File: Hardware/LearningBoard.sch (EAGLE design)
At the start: 55 parts, among them IC1 FT230XS-RFT230XS-R

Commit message: Completed first PCB design ready for OSHPark. REmoved alternate PCB design file created only 1.
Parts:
- removed EXTRA: (no value), pinhead:PINHD-2X5
- D_A: device pinhead:PINHD-1X6 -> pinhead:PINHD-1X8
- I2C: device pinhead:PINHD-1X5 -> pinhead:PINHD-1X6
- UART: device pinhead:PINHD-1X4 -> pinhead:PINHD-1X5
- renumbered BTN4 to T_STMP
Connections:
- net N$28 renamed DIN
- removed net N$31: RPU5.2, U$11.OS
- new net OS: I2C.5, RPU5.2, U$11.OS
- new net VDD_I2C: C1.1, I2C.6, RPU16.2, RPU17.2, RPU5.1, U$11.VCC, U$2.VDD
- new net VDD_IR: RECEIVER_.C, RPU12.2, TRANSMITTER.4
- new net VDD_SPI: C3.1, RPU4.1, SPI.7, U$1.VDD
- new net VDD_UART: C10.1, C5.1, C8.1, C9.1, IC1.!RESET, IC1.3V3OUT, IC1.VCC, IC1.VCCIO, UART.5
- net LEFT_BTN: now also D_A.3; no longer D_A.2
- net MISO: now also SPI.4, U$1.SDO; no longer SPI.3, U$1.SDI
- net MOSI: now also SPI.3, U$1.SDI; no longer SPI.4, U$1.SDO
- net POT_OUT: now also D_A.2; no longer D_A.1
- net RIGHT_BTN: now also D_A.5; no longer D_A.3
- net UP_BTN: now also D_A.6; no longer D_A.5
- net VDD: now also D_A.8; no longer C1.1, C10.1, C3.1, C5.1, C8.1, C9.1, EXTRA.10, EXTRA.2, EXTRA.4, EXTRA.6, EXTRA.8, I2C.5, IC1.!RESET, IC1.3V3OUT, IC1.VCC, IC1.VCCIO, RECEIVER_.C, RPU12.2, RPU16.2, RPU17.2, RPU4.1, RPU5.1, SPI.7, TRANSMITTER.4, U$1.VDD, U$11.VCC, U$2.VDD
- net VIN: now also D_A.7; no longer D_A.6
- net VSS: now also D_A.1; no longer EXTRA.1, EXTRA.3, EXTRA.5, EXTRA.7, EXTRA.9
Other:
- note removed: "EXTRA"
- moved on the sheet: DOWN, IC1, LEFT, RIGHT, UP

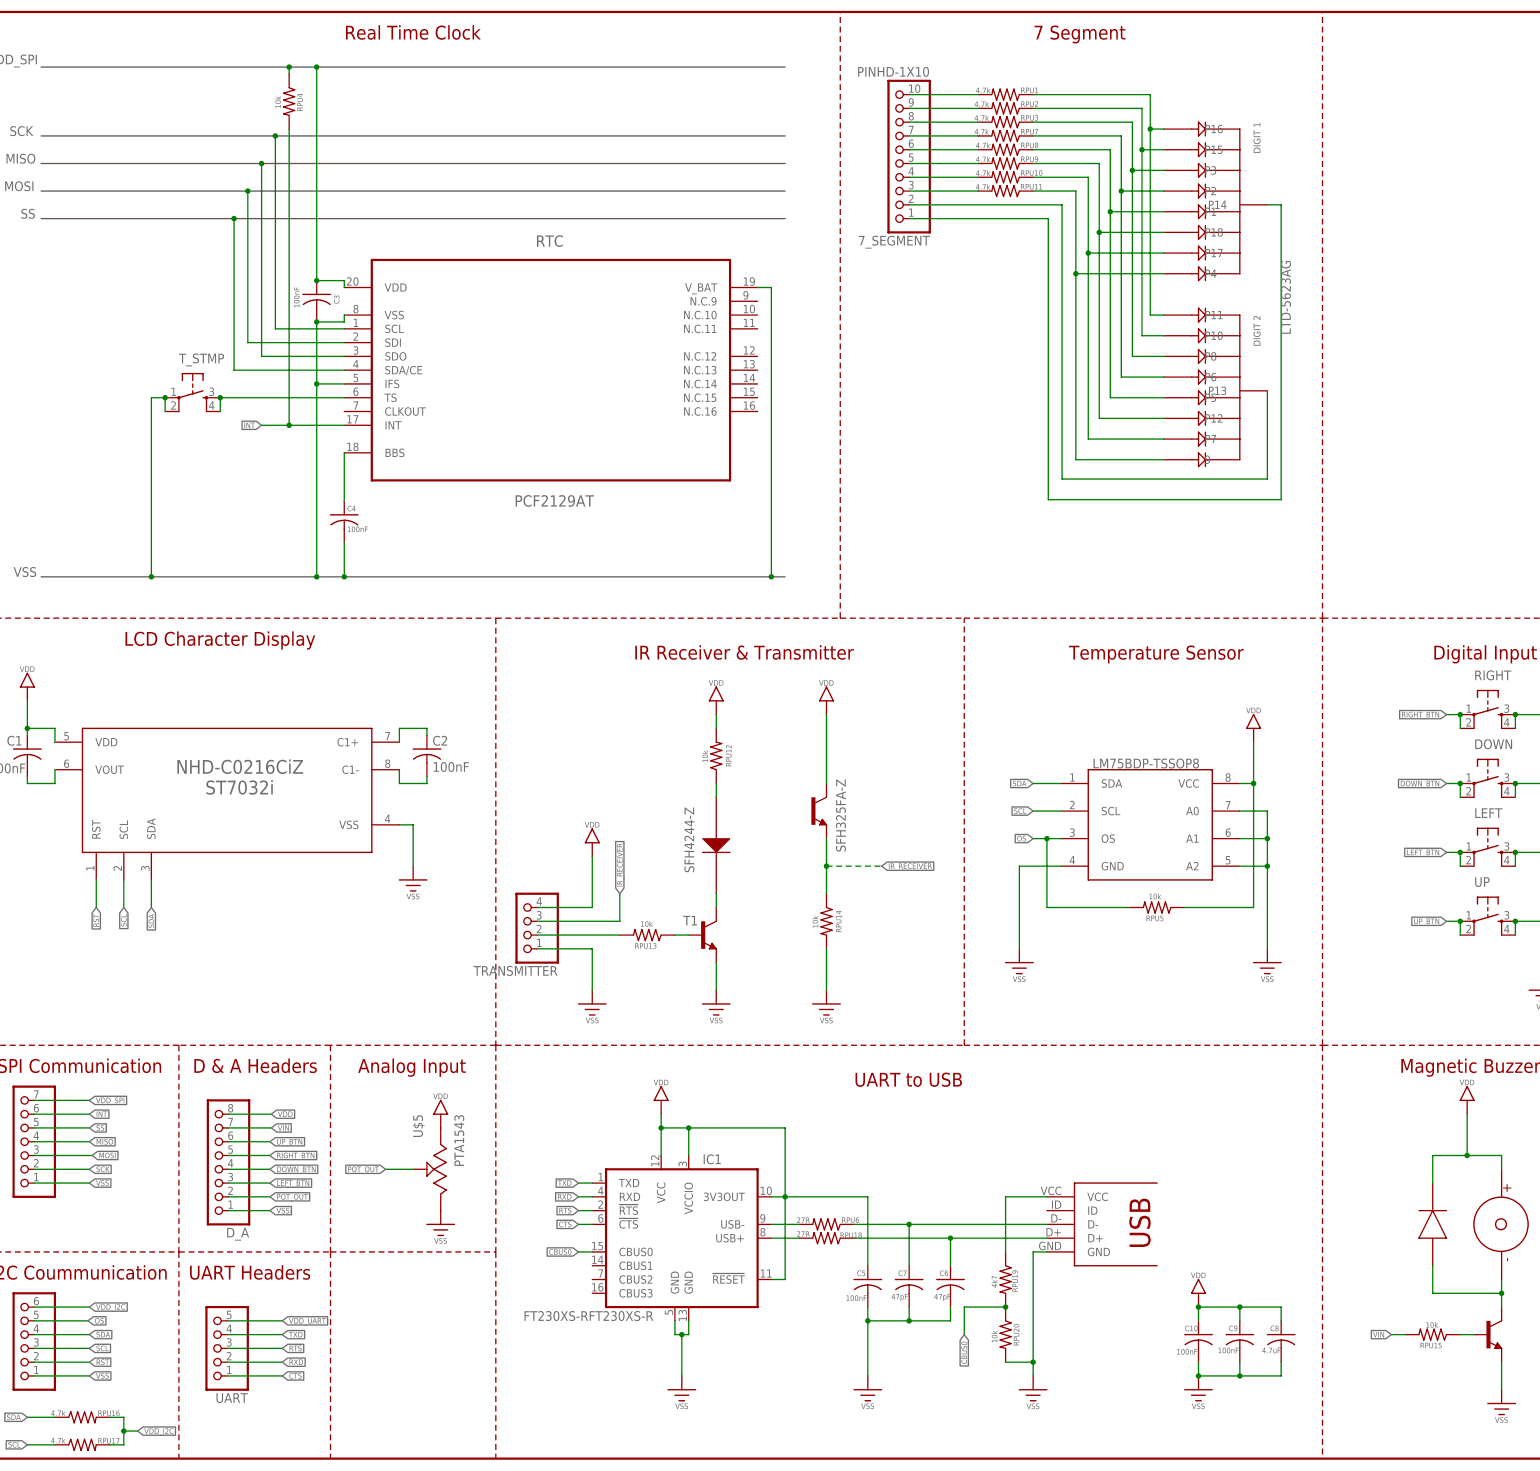
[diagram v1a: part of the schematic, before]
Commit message: - Added some resistor values - Changed resistor names (removed UP string).
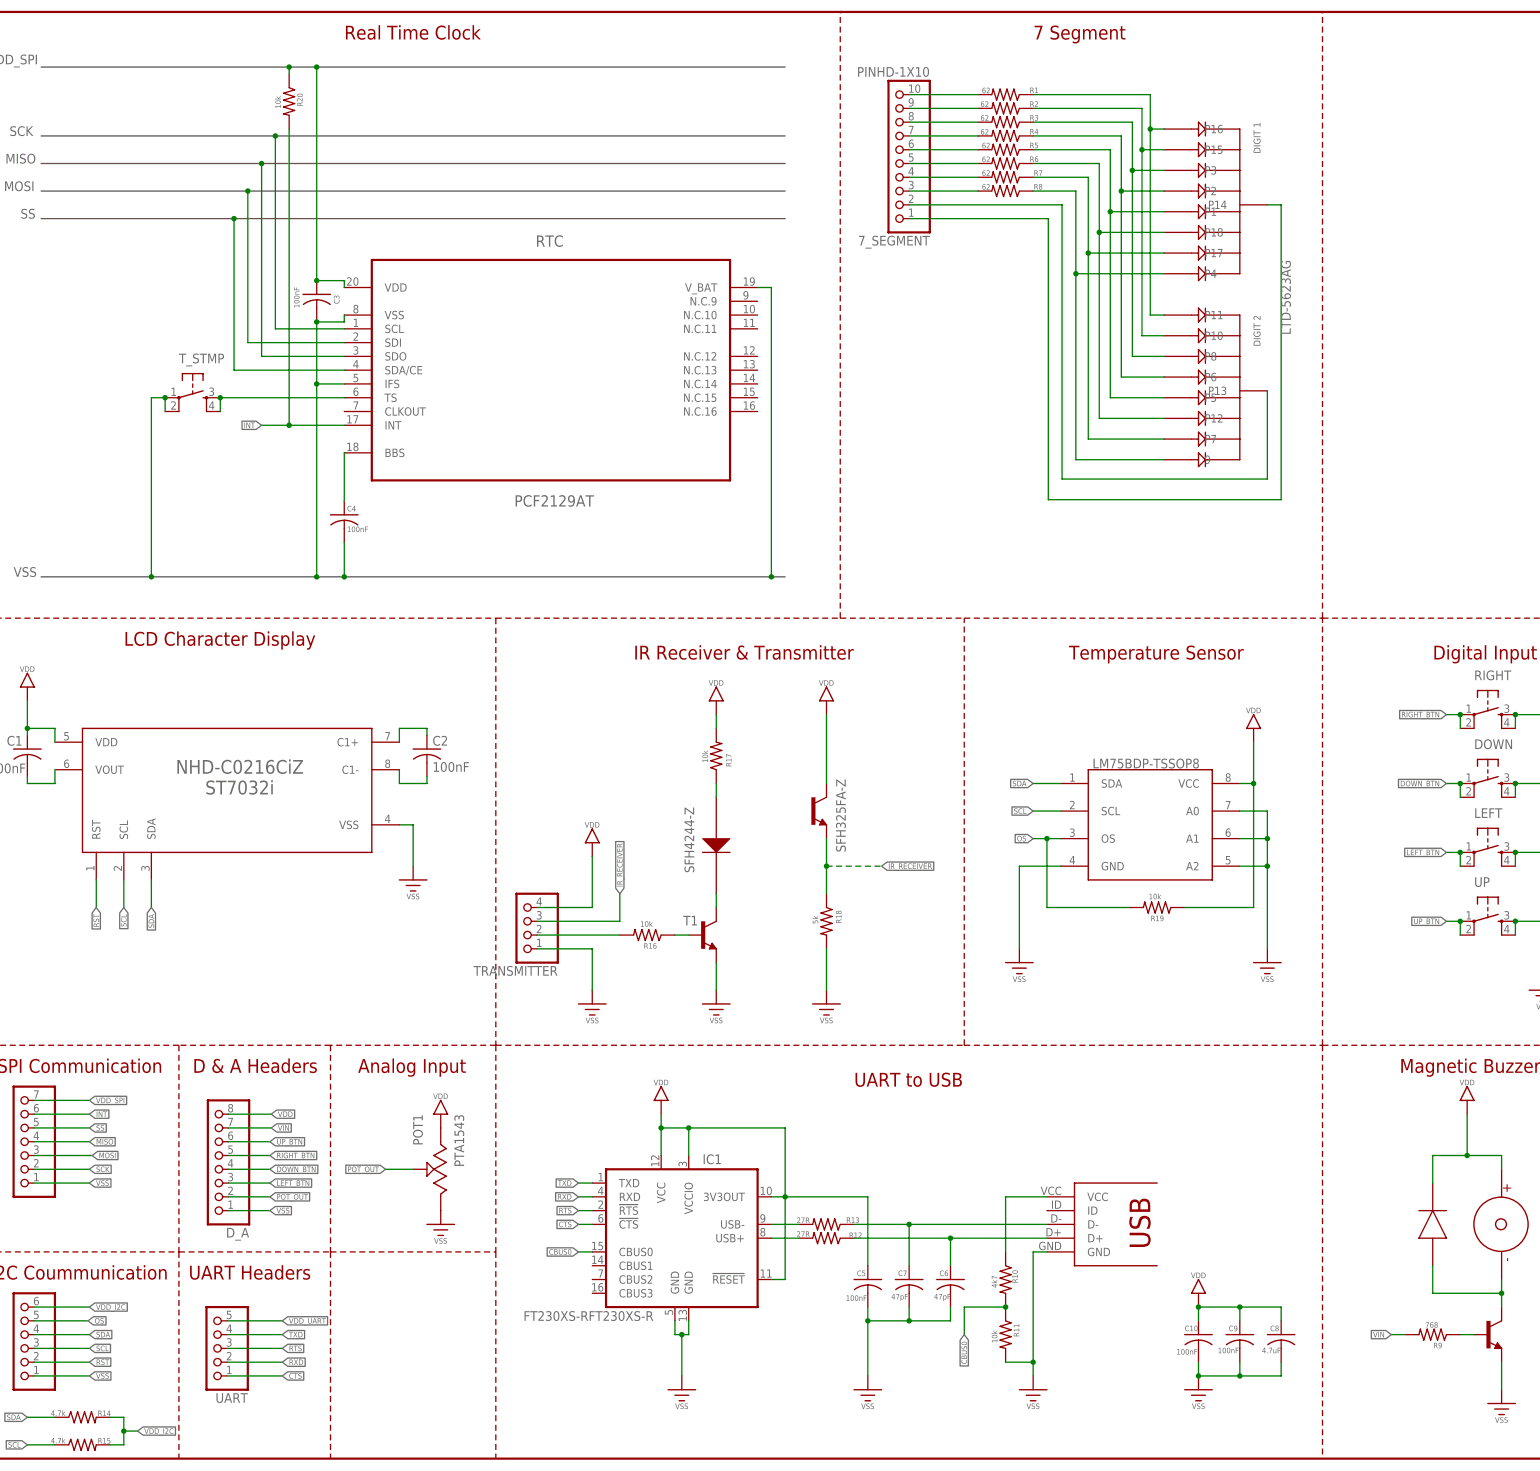
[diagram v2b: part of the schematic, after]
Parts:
- R1, R2, R3, R4, R5, R6, R7, R8: value 4.7k -> 62
- R18: value 10k -> 5k
- R9: value 10k -> 768
- renumbered RPU1 to R1, RPU10 to R7, RPU11 to R8, RPU12 to R17, RPU13 to R16, RPU14 to R18, RPU15 to R9, RPU16 to R14, RPU17 to R15, RPU18 to R12, RPU19 to R10, RPU2 to R2, RPU20 to R11, RPU3 to R3, RPU4 to R20, RPU5 to R19, RPU6 to R13, RPU7 to R4, RPU8 to R5, RPU9 to R6, U$5 to POT1

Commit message: New slim design.
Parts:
- removed T2: (no value), transistor:MMBT3904LT1-NPN-SOT23-BEC
- removed U$8: 254-EMB-140-RO, AllAboutEE:254-EMB-140-RO
- removed U$9: 1N4148X-TP, AllAboutEE:1N4148X-TP
- added LED1: (no value), SparkFun-LED:LED5MM
- added VSS: VSS, pinhead:PINHD-1X1
- D_A: device pinhead:PINHD-1X8 -> pinhead:PINHD-1X7
- I2C: device pinhead:PINHD-1X6 -> pinhead:PINHD-1X5
- R10: value 4k7 -> 4.7k
- R16: value 10k -> 510
- R17: value 10k -> 30
- R9: value 768 -> 1k
- SPI: device pinhead:PINHD-1X7 -> pinhead:PINHD-1X6
- TRANSMITTER: device pinhead:PINHD-1X4 -> pinhead:PINHD-1X3
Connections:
- removed net N$29: R9.1, T2.B
- removed net VIN: D_A.7, R9.2
- new net PWM: D_A.6, R9.2
- net CTS: now also UART.4; no longer UART.1
- net DIN: now also TRANSMITTER.1; no longer TRANSMITTER.2
- net DOWN_BTN: now also D_A.2; no longer D_A.4
- net INT: now also SPI.5; no longer SPI.6
- net IR_RECEIVER: now also TRANSMITTER.2; no longer TRANSMITTER.3
- net LEFT_BTN: now also D_A.5; no longer D_A.3
- net MISO: now also SPI.3; no longer SPI.4
- net MOSI: now also SPI.2; no longer SPI.3
- net N$4: now also LED1.A, R9.1; no longer T2.C, U$8.NEGATIVE, U$9.A
- net OS: now also I2C.4; no longer I2C.5
- net POT_OUT: now also D_A.1; no longer D_A.2
- net RIGHT_BTN: now also D_A.3; no longer D_A.5
- net RST: now also I2C.1; no longer I2C.2
- net RTS: now also UART.2; no longer UART.3
- net RXD: now also UART.3; no longer UART.2
- net SCK: now also SPI.1; no longer SPI.2
- net SCL: now also I2C.2; no longer I2C.3
- net SDA: now also I2C.3; no longer I2C.4
- net SS: now also SPI.4; no longer SPI.5
- net TXD: now also UART.1; no longer UART.4
- net UP_BTN: now also D_A.4; no longer D_A.6
- net VDD: now also D_A.7; no longer D_A.8, U$8.POSITIVE, U$9.C
- net VDD_I2C: now also I2C.5; no longer I2C.6
- net VDD_IR: now also TRANSMITTER.3; no longer TRANSMITTER.4
- net VDD_SPI: now also SPI.6; no longer SPI.7
- net VSS: now also LED1.C, VSS.1; no longer D_A.1, I2C.1, SPI.1, T2.E, TRANSMITTER.1
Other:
- note added: "GND"
- note added: "PWM LED"
- note removed: "Magnetic Buzzer"
- moved on the sheet: R14, R15, R9, UART
